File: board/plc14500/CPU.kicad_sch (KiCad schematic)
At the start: 73 parts, among them U10 MC14500, U11 74HC14, U3 74HC14, U7 74HC590A, U8 LH5168, U9 NE555

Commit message: Rearrange LEDs
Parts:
- added D50, D52, D53: LED 3MM Red, plc14500:LED_3MM, symbol plc14500-rescue:LED5MM-SparkFun-LED
- added R56, R67: 820R, Resistor_THT:R_Axial_DIN0204_L3.6mm_D1.6mm_P7.62mm_Horizontal, symbol Device:R
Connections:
- net GND: now also R53.1, R56.1, R67.1
- net at U10.10 (FLAG0): now also D52.A
- net at U10.11 (RTN): now also D50.A
- net CLK1: now reaches U10.14 (X1)
- net CLK1: now also U7.11 (CPC), U7.13 (CPR); no longer R53.1
- net at U10.9 (FLAGF): now also D53.A
- net CLK renamed CLK2
- net CLK2: no longer R53.2, U7.11 (CPC), U7.13 (CPR)
- new net: D50.K (C), R53.2
- new net: D53.K (C), R67.2
- new net: D52.K (C), R56.2
- no-connect marks 5 -> 2

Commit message: REV.D Schema updates
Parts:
- S16, S18: symbol plc14500-rescue:SWITCH-DPDT-PTH-GPI-152-3013-SparkFun-Switches -> plc14500:SWITCH-DPDT
- U11, U3: symbol 74xx:74HC14 -> plc14500:74HC14
- U7: symbol 74xx:74HC590A -> plc14500:74HC590A
- U8: symbol Memory_RAM:KM62256CLP -> plc14500:KM62256CLP
- U9: symbol plc14500-rescue:555D-SparkFun-IC-Special-Function -> plc14500:555
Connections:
- net at R30.1, U9.7 (DIS): now also R31.2; no longer R31.1
- net at C10.1, U9.2 (TRI), U9.6 (TRE): now also R31.1, S16.7; no longer R31.2, S16.5
- net at U9.3 (OUT): now also S18.1; no longer S18.3
- net at U3.8: now also S18.3; no longer S18.1
- net at S18.5: now also D28.A; no longer D33.A
- net at S18.7: now also D33.A; no longer D28.A
- net at S16.1: now also R29.1; no longer R28.1
- net at S16.3: now also R28.1; no longer R29.1
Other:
- note added: "Program Memory"
- note removed: "Memory"
- moved on the sheet: C10, C11, C12, C13, C14, C7, C8, C9, D18, D19, D20, D21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

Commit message: Address ERC errors
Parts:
- C7: symbol plc14500-rescue:CP-Device -> plc14500:CP-Device
- D18, D19, D20, D21, D22, D23, D24, D25, D26, D27, D28, D29, D30, D31, D32, D33, D34, D35, D36, D37, D38, D39, D41, D42, D50, D52, D53: footprint plc14500:LED_3MM -> LED_5MM; symbol plc14500-rescue:LED5MM-SparkFun-LED -> plc14500:LED
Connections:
- net WEN renamed !WEN

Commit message: Cleanup, ready to route
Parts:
- D18, D19, D20, D21, D22, D23, D24, D25, D26, D27, D28, D29, D30, D31, D32, D33, D34, D35, D36, D37, D38, D39, D41, D42, D50, D52, D53: footprint LED_5MM -> plc14500:LED_3MM; Field4 XXX-00000 -> (none)

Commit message: REV.D first proto
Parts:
- C7: footprint Capacitor_THT:CP_Radial_D8.0mm_P5.00mm -> Capacitor_THT:CP_Radial_D5.0mm_P2.50mm
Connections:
- net GND: now also S16.8 (GND), S16.9 (GND), S18.8 (GND), S18.9 (GND)
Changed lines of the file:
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@@
     (comment 1 "REV.D")
   )
+  (junction (at 177.8 53.34) (diameter 0) (color 0 0 0 0)
+  )
   (junction (at 238.76 45.72) (diameter 0) (color 0 0 0 0)
   )
@@
   (junction (at 195.58 106.68) (diameter 0) (color 0 0 0 0)
   )
+  (junction (at 43.18 62.23) (diameter 0) (color 0 0 0 0)
+  )
   (junction (at 72.39 52.07) (diameter 0) (color 0 0 0 0)
   )
@@
     (stroke (width 0) (type default))
   )
+  (wire (pts (xy 43.18 62.23) (xy 43.18 69.215))
+    (stroke (width 0) (type default))
+  )
   (wire (pts (xy 167.64 34.29) (xy 167.64 43.18))
     (stroke (width 0) (type default))
@@
     (stroke (width 0) (type default))
   )
+  (wire (pts (xy 176.53 53.34) (xy 177.8 53.34))
+    (stroke (width 0) (type default))
+  )
   (wire (pts (xy 87.63 144.78) (xy 96.52 144.78))
     (stroke (width 0) (type default))
@@
     (stroke (width 0) (type default))
   )
+  (wire (pts (xy 41.91 62.23) (xy 43.18 62.23))
+    (stroke (width 0) (type default))
+  )
   (wire (pts (xy 100.33 109.22) (xy 104.14 109.22))
     (stroke (width 0) (type default))
@@
     (stroke (width 0) (type default))
   )
+  (wire (pts (xy 43.18 62.23) (xy 44.45 62.23))
+    (stroke (width 0) (type default))
+  )
   (wire (pts (xy 72.39 52.07) (xy 74.93 52.07))
     (stroke (width 0) (type default))
@@
     (stroke (width 0) (type default))
   )
+  (wire (pts (xy 177.8 53.34) (xy 179.07 53.34))
+    (stroke (width 0) (type default))
+  )
   (wire (pts (xy 233.68 54.61) (xy 233.68 52.07))
     (stroke (width 0) (type default))
@@
     (stroke (width 0) (type default))
   )
+  (wire (pts (xy 177.8 53.34) (xy 177.8 67.945))
+    (stroke (width 0) (type default))
+  )
   (wire (pts (xy 110.49 53.34) (xy 110.49 36.83))
     (stroke (width 0) (type default))
@@
   (symbol (lib_id "plc14500:CP-Device") (at 34.29 64.77 0) (unit 1)
     (in_bom yes) (on_board yes) (dnp no)
-    (property "Reference" "C7" (at 37.2872 63.6016 0)
+    (property "Reference" "C7" (at 27.305 65.6336 0)
       (effects (font (size 1.27 1.27)) (justify left))
     )
-    (property "Value" "470uF" (at 37.2872 65.913 0)
+    (property "Value" "470uF" (at 27.305 67.945 0)
       (effects (font (size 1.27 1.27)) (justify left))
     )
-    (property "Footprint" "Capacitor_THT:CP_Radial_D8.0mm_P5.00mm" (at 35.2552 68.58 0)
+    (property "Footprint" "Capacitor_THT:CP_Radial_D5.0mm_P2.50mm" (at 35.2552 68.58 0)
       (effects (font (size 1.27 1.27)) hide)
     )
@@
     )
   )
-  (symbol (lib_id "plc14500:SWITCH-DPDT") (at 177.8 43.18 180) (unit 1)
+  (symbol (lib_name "SWITCH-DPDT_1") (lib_id "plc14500:SWITCH-DPDT") (at 177.8 43.18 180) (unit 1)
     (in_bom yes) (on_board yes) (dnp no)
-    (property "Reference" "S18" (at 177.8 31.242 0)
+    (property "Reference" "S18" (at 173.355 31.75 0)
       (effects (font (size 1.143 1.143)))
     )
@@
     (pin "6")
     (pin "7")
+    (pin "8")
+    (pin "9")
     (instances
       (project "plc14500"
@@
     (pin "6")
     (pin "7")
+    (pin "8")
+    (pin "9")
     (instances
       (project "plc14500"
@@
     )
   )
+  (symbol (lib_id "power:GND") (at 43.18 69.215 0) (unit 1)
+    (in_bom yes) (on_board yes) (dnp no)
+    (property "Reference" "#PWR01" (at 43.18 75.565 0)
+      (effects (font (size 1.27 1.27)) hide)
+    )
+    (property "Value" "GND" (at 43.307 73.6092 0)
+      (effects (font (size 1.27 1.27)) hide)
+    )
+    (property "Footprint" "" (at 43.18 69.215 0)
+      (effects (font (size 1.27 1.27)) hide)
+    )
+    (property "Datasheet" "" (at 43.18 69.215 0)
+      (effects (font (size 1.27 1.27)) hide)
+    )
+    (pin "1")
+    (instances
+      (project "plc14500"
+        (path "/e5c24396-229a-4727-a88d-8f28d7f70179/00000000-0000-0000-0000-00006394a5b3"
+          (reference "#PWR01") (unit 1)
+        )
+        (path "/e5c24396-229a-4727-a88d-8f28d7f70179"
+          (reference "#PWR?") (unit 1)
+        )
+      )
+    )
+  )
   (symbol (lib_id "Device:R") (at 185.42 144.78 180) (unit 1)
     (in_bom yes) (on_board yes) (dnp no)
@@
         )
       )
+    )
+  )
+  (symbol (lib_id "power:GND") (at 177.8 67.945 0) (unit 1)
+    (in_bom yes) (on_board yes) (dnp no)
+    (property "Reference" "#PWR02" (at 177.8 74.295 0)
+      (effects (font (size 1.27 1.27)) hide)
+    )
+    (property "Value" "GND" (at 177.927 72.3392 0)
+      (effects (font (size 1.27 1.27)) hide)
+    )
+    (property "Footprint" "" (at 177.8 67.945 0)
+      (effects (font (size 1.27 1.27)) hide)
+    )
+    (property "Datasheet" "" (at 177.8 67.945 0)
+      (effects (font (size 1.27 1.27)) hide)
+    )
+    (pin "1")
+    (instances
+      (project "plc14500"
+        (path "/e5c24396-229a-4727-a88d-8f28d7f70179/00000000-0000-0000-0000-00006394a5b3"
+          (reference "#PWR02") (unit 1)
+        )
+        (path "/e5c24396-229a-4727-a88d-8f28d7f70179"
+          (reference "#PWR?") (unit 1)
+        )
+      )

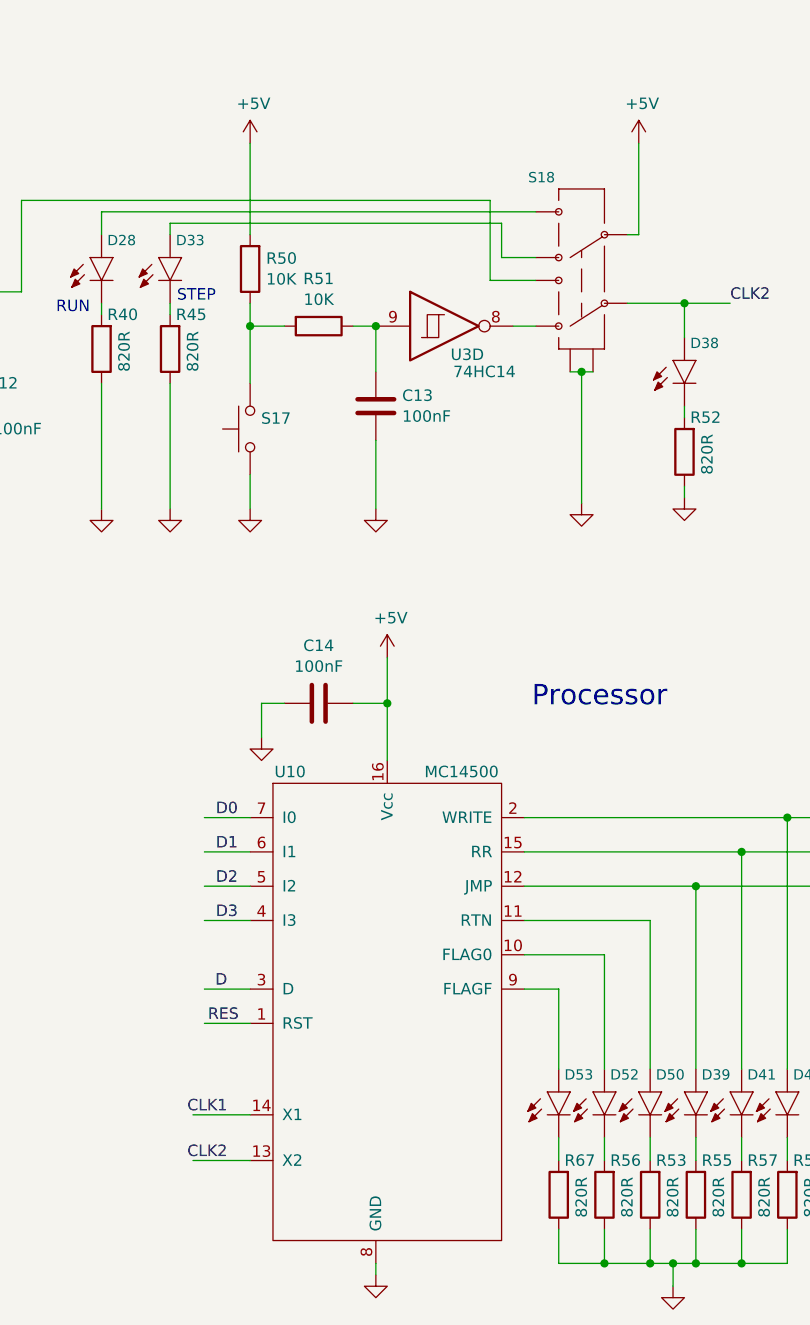
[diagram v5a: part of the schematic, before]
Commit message: Fix issues on REV.D0
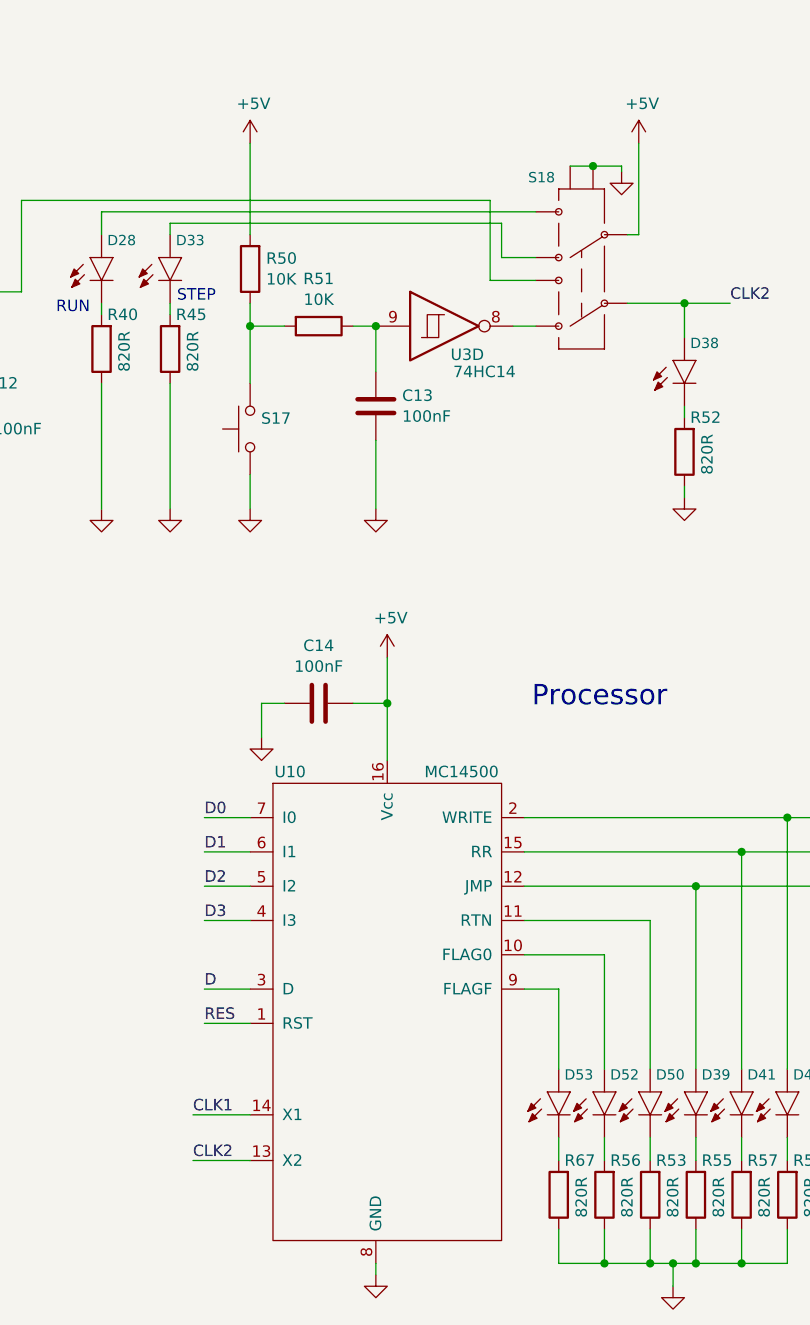
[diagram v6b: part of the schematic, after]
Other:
- moved on the sheet: S18
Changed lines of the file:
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@@
     (comment 1 "REV.D")
   )
-  (junction (at 177.8 53.34) (diameter 0) (color 0 0 0 0)
-  )
   (junction (at 238.76 45.72) (diameter 0) (color 0 0 0 0)
   )
@@
   (junction (at 90.17 82.55) (diameter 0) (color 0 0 0 0)
   )
+  (junction (at 179.07 30.48) (diameter 0) (color 0 0 0 0)
+  )
   (junction (at 259.08 45.72) (diameter 0) (color 0 0 0 0)
   )
@@
     (stroke (width 0) (type default))
   )
+  (wire (pts (xy 176.53 30.48) (xy 179.07 30.48))
+    (stroke (width 0) (type default))
+  )
   (wire (pts (xy 264.16 54.61) (xy 264.16 52.07))
     (stroke (width 0) (type default))
@@
     (stroke (width 0) (type default))
   )
-  (wire (pts (xy 176.53 53.34) (xy 177.8 53.34))
-    (stroke (width 0) (type default))
-  )
   (wire (pts (xy 87.63 144.78) (xy 96.52 144.78))
     (stroke (width 0) (type default))
@@
     (stroke (width 0) (type default))
   )
+  (wire (pts (xy 182.245 30.48) (xy 179.07 30.48))
+    (stroke (width 0) (type default))
+  )
   (wire (pts (xy 87.63 149.86) (xy 96.52 149.86))
     (stroke (width 0) (type default))
@@
     (stroke (width 0) (type default))
   )
+  (wire (pts (xy 182.245 31.115) (xy 182.245 30.48))
+    (stroke (width 0) (type default))
+  )
   (wire (pts (xy 189.23 49.53) (xy 189.23 45.72))
     (stroke (width 0) (type default))
@@
     (stroke (width 0) (type default))
   )
-  (wire (pts (xy 177.8 53.34) (xy 179.07 53.34))
-    (stroke (width 0) (type default))
-  )
   (wire (pts (xy 233.68 54.61) (xy 233.68 52.07))
     (stroke (width 0) (type default))
@@
     (stroke (width 0) (type default))
   )
-  (wire (pts (xy 177.8 53.34) (xy 177.8 67.945))
-    (stroke (width 0) (type default))
-  )
   (wire (pts (xy 110.49 53.34) (xy 110.49 36.83))
     (stroke (width 0) (type default))
@@
     (effects (font (size 1.27 1.27)) (justify left bottom))
   )
-  (label "D0" (at 137.16 102.87 0) (fields_autoplaced)
+  (label "D0" (at 135.89 102.87 0) (fields_autoplaced)
     (effects (font (size 1.27 1.27)) (justify left bottom))
   )
@@
     (effects (font (size 1.27 1.27)) (justify right bottom))
   )
-  (label "D2" (at 137.16 110.49 0) (fields_autoplaced)
+  (label "D2" (at 135.89 110.49 0) (fields_autoplaced)
     (effects (font (size 1.27 1.27)) (justify left bottom))
   )
@@
     (effects (font (size 1.27 1.27)) (justify right bottom))
   )
-  (label "D1" (at 137.16 106.68 0) (fields_autoplaced)
+  (label "D1" (at 135.89 106.68 0) (fields_autoplaced)
     (effects (font (size 1.27 1.27)) (justify left bottom))
   )
@@
     (effects (font (size 1.27 1.27)) (justify left bottom))
   )
-  (label "CLK2" (at 138.43 140.97 180) (fields_autoplaced)
-    (effects (font (size 1.27 1.27)) (justify right bottom))
+  (label "CLK2" (at 134.62 140.97 0) (fields_autoplaced)
+    (effects (font (size 1.27 1.27)) (justify left bottom))
   )
   (label "A4" (at 243.84 21.59 0) (fields_autoplaced)
@@
     (effects (font (size 1.27 1.27)) (justify right bottom))
   )
-  (label "CLK1" (at 138.43 135.89 180) (fields_autoplaced)
-    (effects (font (size 1.27 1.27)) (justify right bottom))
+  (label "CLK1" (at 134.62 135.89 0) (fields_autoplaced)
+    (effects (font (size 1.27 1.27)) (justify left bottom))
   )
   (label "A6" (at 233.68 21.59 0) (fields_autoplaced)
@@
     (effects (font (size 1.27 1.27)) (justify left bottom))
   )
-  (label "D" (at 138.43 121.92 180) (fields_autoplaced)
-    (effects (font (size 1.27 1.27)) (justify right bottom))
+  (label "D" (at 135.89 121.92 0) (fields_autoplaced)
+    (effects (font (size 1.27 1.27)) (justify left bottom))
   )
   (label "D0" (at 29.21 158.75 180) (fields_autoplaced)
@@
     (effects (font (size 1.27 1.27)) (justify left bottom))
   )
-  (label "D3" (at 137.16 114.3 0) (fields_autoplaced)
+  (label "D3" (at 135.89 114.3 0) (fields_autoplaced)
     (effects (font (size 1.27 1.27)) (justify left bottom))
   )
-  (label "RES" (at 139.7 125.73 180) (fields_autoplaced)
-    (effects (font (size 1.27 1.27)) (justify right bottom))
+  (label "RES" (at 135.89 125.73 0) (fields_autoplaced)
+    (effects (font (size 1.27 1.27)) (justify left bottom))
   )
   (label "JMP" (at 33.02 106.68 0) (fields_autoplaced)
@@
     )
   )
-  (symbol (lib_name "SWITCH-DPDT_1") (lib_id "plc14500:SWITCH-DPDT") (at 177.8 43.18 180) (unit 1)
+  (symbol (lib_id "plc14500:SWITCH-DPDT") (at 177.8 43.18 180) (unit 1)
     (in_bom yes) (on_board yes) (dnp no)
     (property "Reference" "S18" (at 173.355 31.75 0)
@@
     )
   )
-  (symbol (lib_id "power:GND") (at 177.8 67.945 0) (unit 1)
+  (symbol (lib_id "power:GND") (at 182.245 31.115 0) (unit 1)
     (in_bom yes) (on_board yes) (dnp no)
-    (property "Reference" "#PWR02" (at 177.8 74.295 0)
+    (property "Reference" "#PWR02" (at 182.245 37.465 0)
       (effects (font (size 1.27 1.27)) hide)
     )
-    (property "Value" "GND" (at 177.927 72.3392 0)
+    (property "Value" "GND" (at 182.372 35.5092 0)
       (effects (font (size 1.27 1.27)) hide)
     )
-    (property "Footprint" "" (at 177.8 67.945 0)
+    (property "Footprint" "" (at 182.245 31.115 0)
       (effects (font (size 1.27 1.27)) hide)
     )
-    (property "Datasheet" "" (at 177.8 67.945 0)
+    (property "Datasheet" "" (at 182.245 31.115 0)
       (effects (font (size 1.27 1.27)) hide)
     )
